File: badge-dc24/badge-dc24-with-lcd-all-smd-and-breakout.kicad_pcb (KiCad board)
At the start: 2 copper layers, 31 parts, among them P1 USB_OTG, U1 ESP-12E, U2 TSOP38238, U3 74HC595, U4 MC78L05ACH

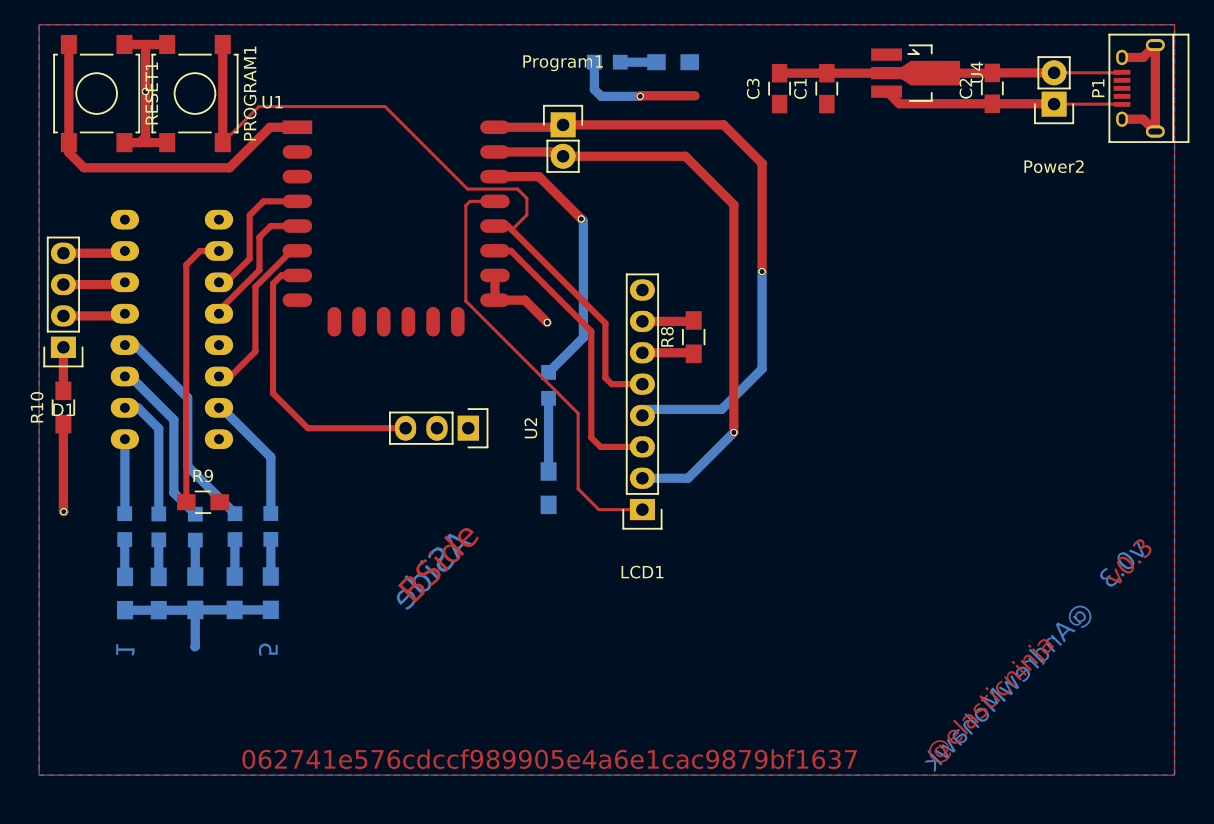
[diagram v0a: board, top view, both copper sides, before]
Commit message: Fixed IR pin-swap and regulator pin-swap
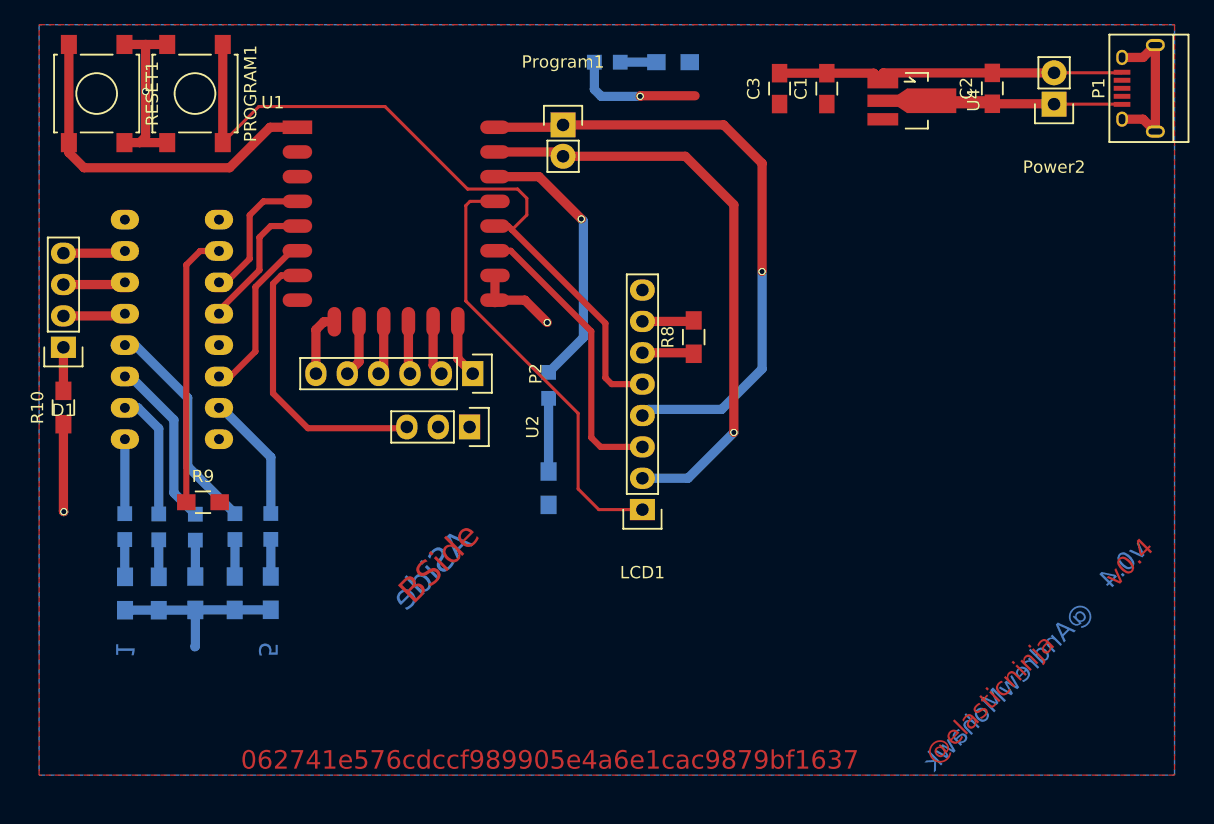
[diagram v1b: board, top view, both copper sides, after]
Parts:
- added P2: CONN_01X06, Pin_Headers:Pin_Header_Straight_1x06, F.Cu at (89.9, 92.2)
- U2: footprint Pin_Headers:Pin_Header_Straight_1x03 -> custom-footprints:IR_Receiver
- U4: footprint TO_SOT_Packages_SMD:SOT89-3_Housing_Handsoldering -> custom-footprints:MC78L05ACH-SOT89-3_Housing_Handsoldering
- moved U4 2.26 mm to (125.5, 70.1)
- moved U2 0.14 mm to (89.7, 96.5)
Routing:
- net Net-(C2-Pad1): track 19.5 -> 30.1 mm
- net Net-(P2-Pad6): track 0.00 -> 5.31 mm
- net GND: track 68.6 -> 73.6 mm
- net Net-(P2-Pad1): track 0.00 -> 4.70 mm
- net Net-(P2-Pad5): track 0.00 -> 4.60 mm
- net Net-(P2-Pad2): track 0.00 -> 4.48 mm
- net Net-(P2-Pad4): track 0.00 -> 4.37 mm
- net Net-(P2-Pad3): track 0.00 -> 4.25 mm
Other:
- board text added: "v0.4"
- board text removed: "v0.3"

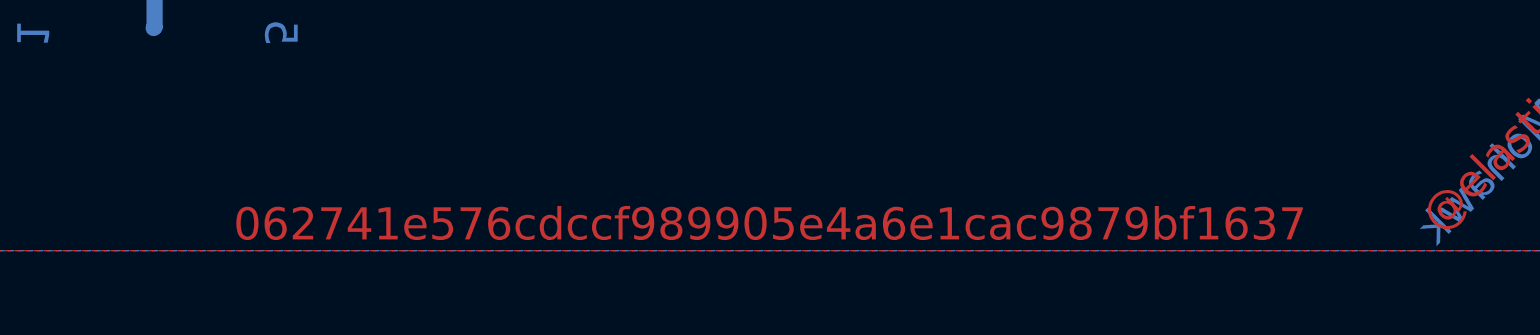
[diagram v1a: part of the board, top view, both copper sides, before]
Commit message: Updated git ref on board
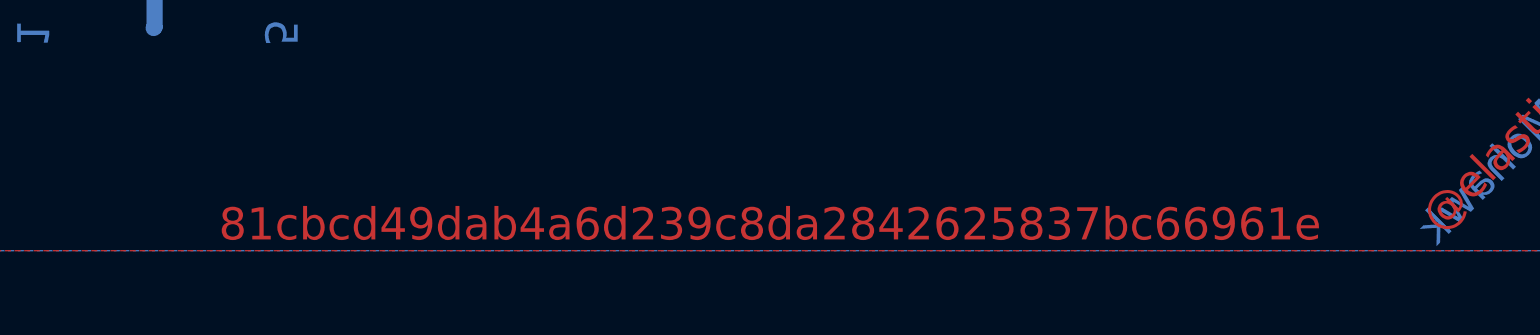
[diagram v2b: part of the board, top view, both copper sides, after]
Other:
- board text added: "81cbcd49dab4a6d239c8da2842625837bc66961e"
- board text removed: "062741e576cdccf989905e4a6e1cac9879bf1637"
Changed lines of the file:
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@@
     (effects (font (size 1.5 1.5) (thickness 0.3)))
   )
-  (gr_text 062741e576cdccf989905e4a6e1cac9879bf1637 (at 96.1644 123.4948) (layer F.Cu)
+  (gr_text 81cbcd49dab4a6d239c8da2842625837bc66961e (at 96.1644 123.4948) (layer F.Cu)
     (effects (font (size 1.5 1.5) (thickness 0.3)))
   )
